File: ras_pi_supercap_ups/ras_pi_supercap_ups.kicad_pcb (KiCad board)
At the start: 2 copper layers, 16 parts, among them J1 Conn_01x03, J3 Conn_01x04, J4 Conn_01x04, J5 Conn_01x05, J6 Conn_01x05, J7 Barrel_Jack_Switch_Pin3Ring, Q1 SUD50P04-08, U1 ATtiny85-20P, U2 TL431LP, U3 TL431LP, U4 TL431LP, U5 TL431LP, U6 TL431LP, U7 LM2596S-5

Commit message: Updated part numbers
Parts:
- added C1: 10F, Capacitor_THT:CP_Radial_D12.5mm_P5.00mm, F.Cu at (32.9, 45.2)
- added C10: 22u 10V X7R, Capacitor_THT:C_Disc_D4.7mm_W2.5mm_P5.00mm, F.Cu at (210.2, 60.8)
- added C2: 10F, Capacitor_THT:CP_Radial_D12.5mm_P5.00mm, F.Cu at (48.6, 45.7)
- added C3: 10F, Capacitor_THT:CP_Radial_D12.5mm_P5.00mm, F.Cu at (64.0, 45.5)
- added C4: 10F, Capacitor_THT:CP_Radial_D12.5mm_P5.00mm, F.Cu at (79.1, 45.5)
- added C5: 10F, Capacitor_THT:CP_Radial_D12.5mm_P5.00mm, F.Cu at (95.8, 46.3)
- added C6: 10u 25V X7R, Capacitor_THT:C_Disc_D4.7mm_W2.5mm_P5.00mm, F.Cu at (202.5, 143.2)
- added C7: 22u 10V X7R, Capacitor_THT:C_Disc_D4.7mm_W2.5mm_P5.00mm, F.Cu at (181.5, 62.0)
- added C8: 22u 10V X7R, Capacitor_THT:C_Disc_D4.7mm_W2.5mm_P5.00mm, F.Cu at (124.5, 136.1)
- added C9: 22u 10V X7R, Capacitor_THT:C_Disc_D4.7mm_W2.5mm_P5.00mm, F.Cu at (139.5, 111.9)
- added D2: SA12A, Diode_THT:D_DO-15_P15.24mm_Horizontal, F.Cu at (118.2, 102.3)
- added D20: Green, LED_THT:LED_D5.0mm, F.Cu at (63.3, 98.6)
- added D3: SA12A, Diode_THT:D_DO-15_P15.24mm_Horizontal, F.Cu at (178.8, 70.6)
- added F1: Fuse_Small, Fuse:Fuse_BelFuse_0ZRE0005FF_L8.3mm_W3.8mm, F.Cu at (89.2, 147.1)
- added F2: Fuse_Small, Fuse:Fuse_BelFuse_0ZRE0005FF_L8.3mm_W3.8mm, F.Cu at (107.6, 144.9)
- added J2: OKR DC/DC, Connector_PinSocket_2.00mm:PinSocket_1x05_P2.00mm_Vertical, F.Cu at (130.0, 111.2)
- added J8: Conn_02x03_Odd_Even, Connector_PinHeader_2.54mm:PinHeader_2x03_P2.54mm_Vertical, F.Cu at (125.7, 111.0)
- added JP1: SolderJumper_2_Open, Jumper:SolderJumper-2_P1.3mm_Open_RoundedPad1.0x1.5mm, F.Cu at (109.7, 150.2)
- added JP2: SolderJumper_2_Open, Jumper:SolderJumper-2_P1.3mm_Open_RoundedPad1.0x1.5mm, F.Cu at (151.2, 105.5)
- added JP3: SolderJumper_2_Open, Jumper:SolderJumper-2_P1.3mm_Open_RoundedPad1.0x1.5mm, F.Cu at (105.4, 150.2)
- added JP4: SolderJumper_2_Open, Jumper:SolderJumper-2_P1.3mm_Open_RoundedPad1.0x1.5mm, F.Cu at (118.4, 110.7)
- added R1: 1k, Resistor_THT:R_Axial_DIN0207_L6.3mm_D2.5mm_P15.24mm_Horizontal, F.Cu at (137.0, 101.8)
- added R10: 267, Resistor_THT:R_Axial_DIN0516_L15.5mm_D5.0mm_P25.40mm_Horizontal, F.Cu at (106.8, 123.0)
- added R11: 10k, Resistor_THT:R_Axial_DIN0207_L6.3mm_D2.5mm_P15.24mm_Horizontal, F.Cu at (88.4, 139.2)
- added R12: 2.2k, Resistor_THT:R_Axial_DIN0207_L6.3mm_D2.5mm_P15.24mm_Horizontal, F.Cu at (88.8, 109.5)
- added R13: 1k, Resistor_THT:R_Axial_DIN0207_L6.3mm_D2.5mm_P15.24mm_Horizontal, F.Cu at (106.8, 114.8)
- added R14: 10k, Resistor_THT:R_Axial_DIN0207_L6.3mm_D2.5mm_P15.24mm_Horizontal, F.Cu at (117.8, 106.9)
- added R2: 1k, Resistor_THT:R_Axial_DIN0207_L6.3mm_D2.5mm_P15.24mm_Horizontal, F.Cu at (88.4, 123.0)
- added R20: 47k, Resistor_THT:R_Axial_DIN0207_L6.3mm_D2.5mm_P15.24mm_Horizontal, F.Cu at (44.0, 96.8)
- added R21: 47k, Resistor_THT:R_Axial_DIN0207_L6.3mm_D2.5mm_P15.24mm_Horizontal, F.Cu at (44.0, 100.9)
- added R3: 1k, Resistor_THT:R_Axial_DIN0207_L6.3mm_D2.5mm_P15.24mm_Horizontal, F.Cu at (88.8, 103.0)
- added R4: 1k, Resistor_THT:R_Axial_DIN0207_L6.3mm_D2.5mm_P15.24mm_Horizontal, F.Cu at (88.4, 118.9)
- added R5: 1k, Resistor_THT:R_Axial_DIN0207_L6.3mm_D2.5mm_P15.24mm_Horizontal, F.Cu at (88.4, 143.2)
- added R6: 1k, Resistor_THT:R_Axial_DIN0207_L6.3mm_D2.5mm_P15.24mm_Horizontal, F.Cu at (106.8, 127.0)
- added R7: 10 3W, Resistor_THT:R_Axial_DIN0516_L15.5mm_D5.0mm_P25.40mm_Horizontal, F.Cu at (106.8, 118.9)
- added R8: 10k, Resistor_THT:R_Axial_DIN0207_L6.3mm_D2.5mm_P15.24mm_Horizontal, F.Cu at (88.4, 114.8)
- added R9: 2.2k, Resistor_THT:R_Axial_DIN0207_L6.3mm_D2.5mm_P15.24mm_Horizontal, F.Cu at (88.4, 127.0)
- added TP1: TestPoint_Small, TestPoint:TestPoint_THTPad_D2.0mm_Drill1.0mm, F.Cu at (113.9, 150.4)
- added TP2: TestPoint_Small, TestPoint:TestPoint_THTPad_D2.0mm_Drill1.0mm, F.Cu at (118.0, 149.2)
- added TP3: TestPoint_Small, TestPoint:TestPoint_THTPad_D2.0mm_Drill1.0mm, F.Cu at (150.5, 129.8)
- added TP4: TestPoint_Small, TestPoint:TestPoint_THTPad_D2.0mm_Drill1.0mm, F.Cu at (122.0, 145.1)
- added TP5: TestPoint_Small, TestPoint:TestPoint_THTPad_D2.0mm_Drill1.0mm, F.Cu at (126.1, 145.1)
- added TP6: TestPoint_Small, TestPoint:TestPoint_THTPad_D2.0mm_Drill1.0mm, F.Cu at (170.2, 101.8)
- added TP7: TestPoint_Small, TestPoint:TestPoint_THTPad_D2.0mm_Drill1.0mm, F.Cu at (151.0, 109.3)
- added TP8: TestPoint_Small, TestPoint:TestPoint_THTPad_D2.0mm_Drill1.0mm, F.Cu at (118.0, 145.1)
- added TP9: TestPoint_Small, TestPoint:TestPoint_THTPad_D2.0mm_Drill1.0mm, F.Cu at (122.0, 149.2)
- added U8: ATtiny85-20P, Package_DIP:DIP-8_W7.62mm, F.Cu at (98.7, 148.5)
- J3, J4: value Conn_01x04 -> Conn_01x05; footprint Connector_PinHeader_2.54mm:PinHeader_1x04_P2.54mm_Vertical -> Connector_PinHeader_2.54mm:PinHeader_1x05_P2.54mm_Vertical
- J5: value Conn_01x05 -> Barrel_Jack_Switch_Pin3Ring; footprint Connector_PinHeader_2.54mm:PinHeader_1x05_P2.54mm_Vertical -> Connector_BarrelJack:BarrelJack_CUI_PJ-063AH_Horizontal
- J6: value Conn_01x05 -> Conn_01x04; footprint Connector_PinHeader_2.54mm:PinHeader_1x05_P2.54mm_Vertical -> Connector_PinHeader_2.54mm:PinHeader_1x04_P2.54mm_Vertical
- J7: value Barrel_Jack_Switch_Pin3Ring -> Conn_01x04; footprint Connector_BarrelJack:BarrelJack_CUI_PJ-063AH_Horizontal -> Connector_PinHeader_2.54mm:PinHeader_1x04_P2.54mm_Vertical
- Q1: value SUD50P04-08 -> IRF5305; footprint Package_TO_SOT_SMD:TO-252-2 -> Package_TO_SOT_THT:TO-220-3_Vertical
- U1: value ATtiny85-20P -> KA431AZTA; footprint Package_DIP:DIP-8_W7.62mm -> Package_TO_SOT_THT:TO-92_Inline
- U2, U3, U4, U5: value TL431LP -> KA431AZTA
- U6: value TL431LP -> LM2596S-5; footprint Package_TO_SOT_THT:TO-92_Inline -> Package_TO_SOT_SMD:TO-263-5_TabPin3
- U7: value LM2596S-5 -> L7805; footprint Package_TO_SOT_SMD:TO-263-5_TabPin3 -> Package_TO_SOT_THT:TO-220-3_Vertical
- moved D1 156.9 mm to (257.8, 114.7)
- moved D5 146.8 mm to (257.5, 79.5)
- moved J1 42.1 mm to (144.7, 33.0), turned to 90 degrees
- moved J6 37.9 mm to (121.5, 32.9), turned to 90 degrees
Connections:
- D5 pad 2: Net-(R1-Pad1) -> Net-(C1-Pad1)
- J3 pad 1: VIN -> POW_OUT
- J3 pad 3: GND -> I2C_SCL
- J3 pad 4: Net-(J3-Pad4) -> I2C_SDA
- J4 pad 1: VIN -> POW_OUT
- J4 pad 3: GND -> I2C_SCL
- J4 pad 4: Net-(J4-Pad4) -> I2C_SDA
- J5 pad 1: POW_OUT -> VIN
- J5 pad 2: GND -> unconnected-(J5-Pad2)
- J6 pad 1: POW_OUT -> VIN
- J6 pad 3: I2C_SCL -> GND
- J6 pad 4: I2C_SDA -> Net-(J6-Pad4)
- J7 pad 2: unconnected-(J7-Pad2) -> GND
- U1 pad 1: RESET -> Net-(C1-Pad1)
- U1 pad 2: VIN_SENSE -> Net-(C1-Pad1)
- U1 pad 3: UPS_SENSE -> Net-(C1-Pad2)
- U2 pad 1: Net-(R1-Pad1) -> Net-(C1-Pad2)
- U2 pad 2: Net-(R1-Pad1) -> Net-(C1-Pad2)
- U5 pad 3: Net-(R4-Pad2) -> GND
- U6 pad 1: Net-(R4-Pad2) -> Net-(C6-Pad1)
- U6 pad 2: Net-(R4-Pad2) -> +5V
- U7 pad 1: Net-(F2-Pad2) -> Net-(C6-Pad1)
- U7 pad 2: +5V -> GND
- U7 pad 3: GND -> Net-(JP1-Pad1)

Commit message: Started updating to SMT
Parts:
- removed F2: Fuse_Small, Fuse:Fuse_BelFuse_0ZRE0005FF_L8.3mm_W3.8mm
- added C11: 22u 10V X7R, Capacitor_SMD:C_0805_2012Metric, F.Cu at (109.7, 112.6)
- added C12: 0.1uF, Capacitor_SMD:C_0805_2012Metric, F.Cu at (109.7, 109.6)
- added H1: MountingHole, MountingHole:MountingHole_2.7mm_M2.5, F.Cu at (54.0, 103.5)
- added H2: MountingHole, MountingHole:MountingHole_2.7mm_M2.5, F.Cu at (114.2, 104.4)
- added H3: MountingHole, MountingHole:MountingHole_2.7mm_M2.5, F.Cu at (53.4, 152.2)
- added H4: MountingHole, MountingHole:MountingHole_2.7mm_M2.5, F.Cu at (111.5, 152.5)
- added J10: Raspberry_Pi_2_3, Connector_PinSocket_2.54mm:PinSocket_2x20_P2.54mm_Vertical, B.Cu at (59.6, 105.2)
- added J9: LEDs and Buttons, Connector_PinHeader_2.54mm:PinHeader_1x08_P2.54mm_Vertical, F.Cu at (16.7, 114.8)
- added U9: STC8H1K08, Package_SO:TSSOP-20_4.4x5mm_P0.5mm, F.Cu at (103.1, 111.3)
- C10, C6, C7, C8, C9: footprint Capacitor_THT:C_Disc_D4.7mm_W2.5mm_P5.00mm -> Capacitor_SMD:C_0805_2012Metric
- D1, D5: value 1N5820 -> B340LA-13-F; footprint Diode_THT:D_DO-201AD_P15.24mm_Horizontal -> Diode_SMD:D_SMA
- D2, D3: value SA12A -> PTVSHC3D15VUH; footprint Diode_THT:D_DO-15_P15.24mm_Horizontal -> Diode_SMD:D_SOD-323
- D20: footprint LED_THT:LED_D5.0mm -> LED_SMD:LED_0805_2012Metric
- F1: footprint Fuse:Fuse_BelFuse_0ZRE0005FF_L8.3mm_W3.8mm -> Fuse:Fuse_1206_3216Metric
- Q1: footprint Package_TO_SOT_THT:TO-220-3_Vertical -> Package_TO_SOT_SMD:TO-263-2
- R1, R2, R3, R4, R5: footprint Resistor_THT:R_Axial_DIN0207_L6.3mm_D2.5mm_P15.24mm_Horizontal -> Resistor_SMD:R_1206_3216Metric
- R10: footprint Resistor_THT:R_Axial_DIN0516_L15.5mm_D5.0mm_P25.40mm_Horizontal -> Resistor_SMD:R_0805_2012Metric
- R11, R12, R13, R14, R20, R21, R6, R8, R9: footprint Resistor_THT:R_Axial_DIN0207_L6.3mm_D2.5mm_P15.24mm_Horizontal -> Resistor_SMD:R_0805_2012Metric
- moved D5 180.9 mm to (81.1, 119.8)
- moved D1 152.9 mm to (105.0, 118.0)
- moved J6 151.9 mm to (15.2, 141.4)
- moved J7 142.6 mm to (18.8, 100.6)
- moved J1 139.9 mm to (17.7, 91.5)
- moved C10 132.0 mm to (99.5, 132.6)
- moved C1 124.0 mm to (111.0, 141.6), turned to 180 degrees
- moved C6 123.8 mm to (80.0, 124.6), turned to -90 degrees
- moved J4 119.3 mm to (25.0, 122.9)
- moved J3 115.0 mm to (17.9, 121.7)
- moved Q1 113.0 mm to (57.3, 119.0), turned to 90 degrees
- moved JP2 109.6 mm to (43.3, 86.2)
- moved C7 107.8 mm to (94.6, 126.0)
- moved C2 107.8 mm to (97.9, 141.6), turned to 180 degrees
- moved U3 106.6 mm to (85.7, 151.8), turned to 180 degrees
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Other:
- board outline added: 85 x 56 mm

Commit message: Updates
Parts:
- removed J5: Barrel_Jack_Switch_Pin3Ring, Connector_BarrelJack:BarrelJack_CUI_PJ-063AH_Horizontal
- removed JP2: SolderJumper_2_Open, Jumper:SolderJumper-2_P1.3mm_Open_RoundedPad1.0x1.5mm
- removed R10: 267, Resistor_SMD:R_0805_2012Metric
- added J12: 171826-4, raspberrypi_supercap_ups_lib:TE_171826-4, F.Cu at (111.2, 128.1)
- J1: value Conn_01x03 -> Raspberry_Pi_2_3; footprint Connector_PinHeader_2.54mm:PinHeader_1x03_P2.54mm_Vertical -> Connector_PinSocket_2.54mm:PinSocket_2x20_P2.54mm_Vertical; moved to B.Cu
- J10: value Raspberry_Pi_2_3 -> Conn_01x03; footprint Connector_PinSocket_2.54mm:PinSocket_2x20_P2.54mm_Vertical -> Connector_PinHeader_2.54mm:PinHeader_1x03_P2.54mm_Vertical
- J2: value OKR DC/DC -> Raspberry_Pi_2_3; footprint Connector_PinSocket_2.00mm:PinSocket_1x05_P2.00mm_Vertical -> Connector_PinSocket_2.54mm:PinSocket_2x20_P2.54mm_Vertical; moved to B.Cu
- JP1, JP3, JP4: moved to B.Cu
- moved R7 109.2 mm to (157.0, 100.8), turned to -90 degrees
- moved U7 76.5 mm to (70.5, 132.7)
- moved J8 72.7 mm to (110.5, 108.9)
- moved TP7 63.6 mm to (130.4, 143.3)
- moved TP3 57.3 mm to (130.4, 149.5)
- moved TP6 57.1 mm to (133.7, 143.6)
- moved JP1 45.6 mm to (73.6, 126.8), turned to 180 degrees
- moved D2 44.9 mm to (89.0, 117.9)
- moved J1 42.7 mm to (58.3, 104.8), turned to -90 degrees
- moved U8 39.9 mm to (30.0, 124.9)
- moved J10 39.2 mm to (95.9, 90.3)
- moved J3 37.2 mm to (53.0, 109.4)
- moved JP3 36.9 mm to (77.9, 126.8), turned to 180 degrees
- moved J2 34.2 mm to (58.3, 112.4), turned to -90 degrees
- moved D3 22.8 mm to (72.8, 122.2)
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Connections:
- J1 pad 1: Net-(D1-Pad1) -> +3V3
- J1 pad 2: Net-(J1-Pad2) -> POW_OUT
- J1 pad 3: GND -> I2C_SCL
- J10 pad 1: unconnected-(J10-Pad1) -> Net-(D1-Pad1)
- J10 pad 2: POW_OUT -> Net-(J10-Pad2)
- J10 pad 3: I2C_SCL -> GND
- J2 pad 1: unconnected-(J2-Pad1) -> +3V3
- J2 pad 2: Net-(C6-Pad1) -> POW_OUT
- J2 pad 3: GND -> I2C_SCL
- J2 pad 4: Net-(J2-Pad4) -> POW_OUT
- J2 pad 5: Net-(J2-Pad5) -> I2C_SDA
- R7 pad 1: Net-(J1-Pad2) -> Net-(J10-Pad2)
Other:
- board size 85 x 56 mm -> 65 x 56 mm

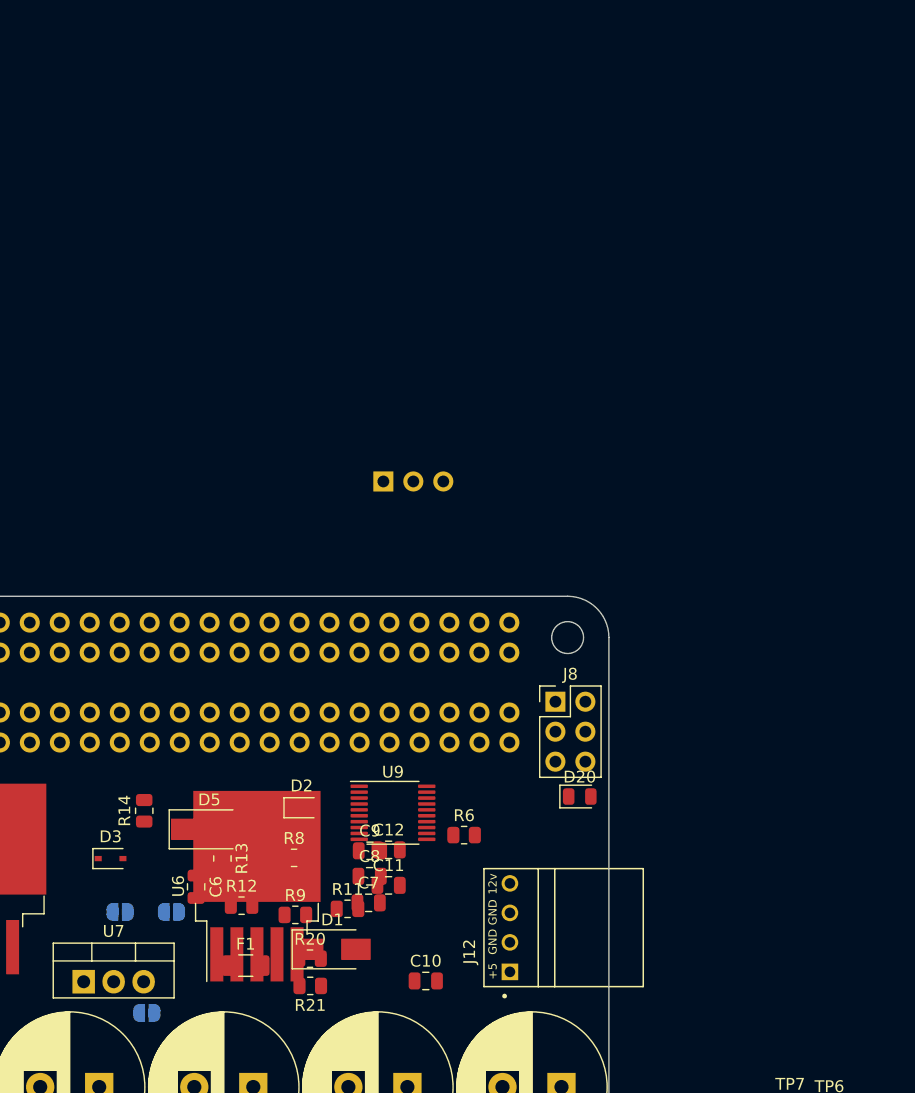
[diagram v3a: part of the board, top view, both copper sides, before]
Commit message: Added simple buck converter
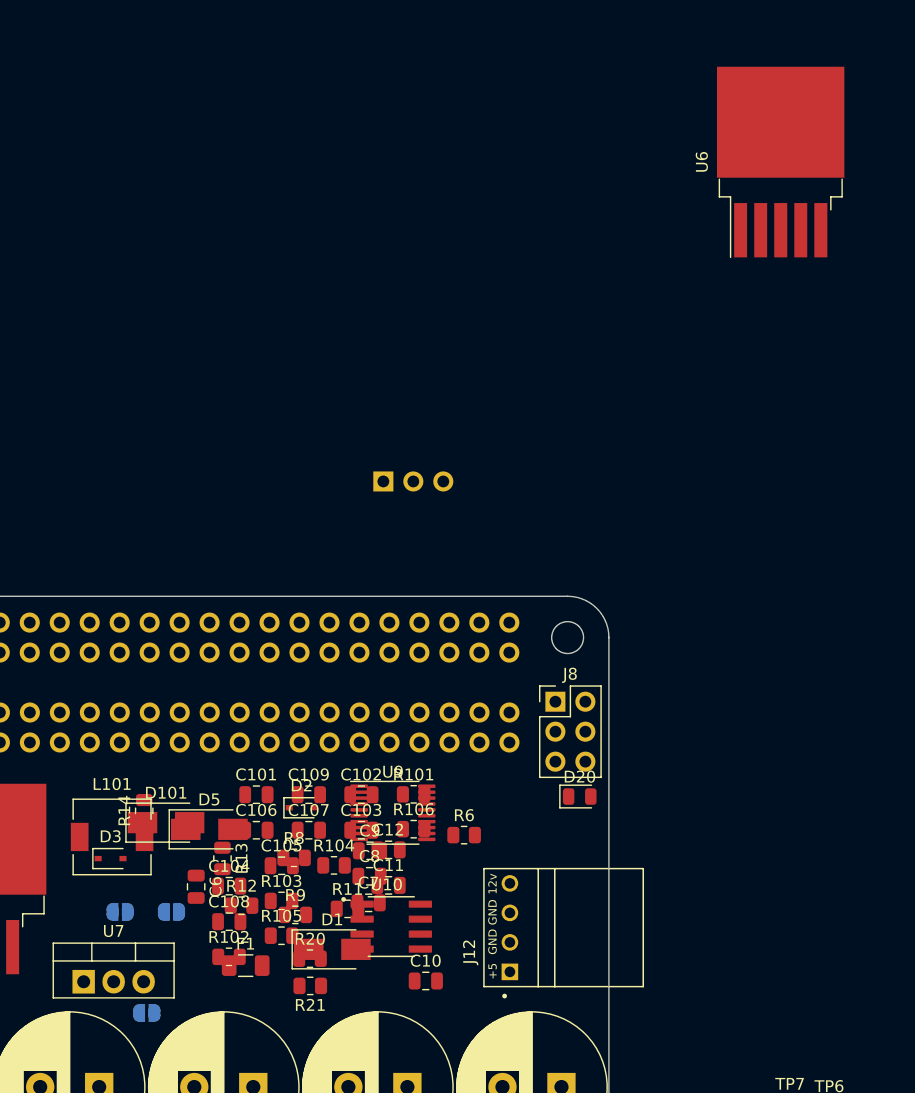
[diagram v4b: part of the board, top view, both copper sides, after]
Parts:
- added C101: 4.7u, Capacitor_SMD:C_0805_2012Metric, F.Cu at (85.1, 116.8)
- added C102: 4.7u, Capacitor_SMD:C_0805_2012Metric, F.Cu at (94.0, 116.8)
- added C103: 0.01u, Capacitor_SMD:C_0805_2012Metric, F.Cu at (94.0, 119.8)
- added C104: 0.1u, Capacitor_SMD:C_0805_2012Metric, F.Cu at (82.8, 124.6)
- added C105: 0.01u, Capacitor_SMD:C_0805_2012Metric, F.Cu at (87.3, 122.8)
- added C106: 1000p, Capacitor_SMD:C_0805_2012Metric, F.Cu at (85.1, 119.8)
- added C107: 47p, Capacitor_SMD:C_0805_2012Metric, F.Cu at (89.6, 119.8)
- added C108: 47u, Capacitor_SMD:C_0805_2012Metric, F.Cu at (82.8, 127.6)
- added C109: 47u, Capacitor_SMD:C_0805_2012Metric, F.Cu at (89.6, 116.8)
- added D101: B340A, Diode_SMD:D_SMA, F.Cu at (77.5, 119.2)
- added L101: 6.8uH, Inductor_SMD:L_6.3x6.3_H3, F.Cu at (72.9, 120.4)
- added R101: 332k, Resistor_SMD:R_0805_2012Metric, F.Cu at (98.5, 116.8)
- added R102: 68.1k, Resistor_SMD:R_0805_2012Metric, F.Cu at (82.8, 130.6)
- added R103: 29.4k, Resistor_SMD:R_0805_2012Metric, F.Cu at (87.3, 125.8)
- added R104: 0, Resistor_SMD:R_0805_2012Metric, F.Cu at (91.7, 122.8)
- added R105: 10.2k, Resistor_SMD:R_0805_2012Metric, F.Cu at (87.3, 128.8)
- added R106: 3.24k, Resistor_SMD:R_0805_2012Metric, F.Cu at (98.5, 119.7)
- added U10: TPS54331DR, raspberrypi_supercap_ups_lib:SOIC127P599X175-8N, F.Cu at (96.6, 128.0)
- moved U6 75.7 mm to (129.6, 63.2)

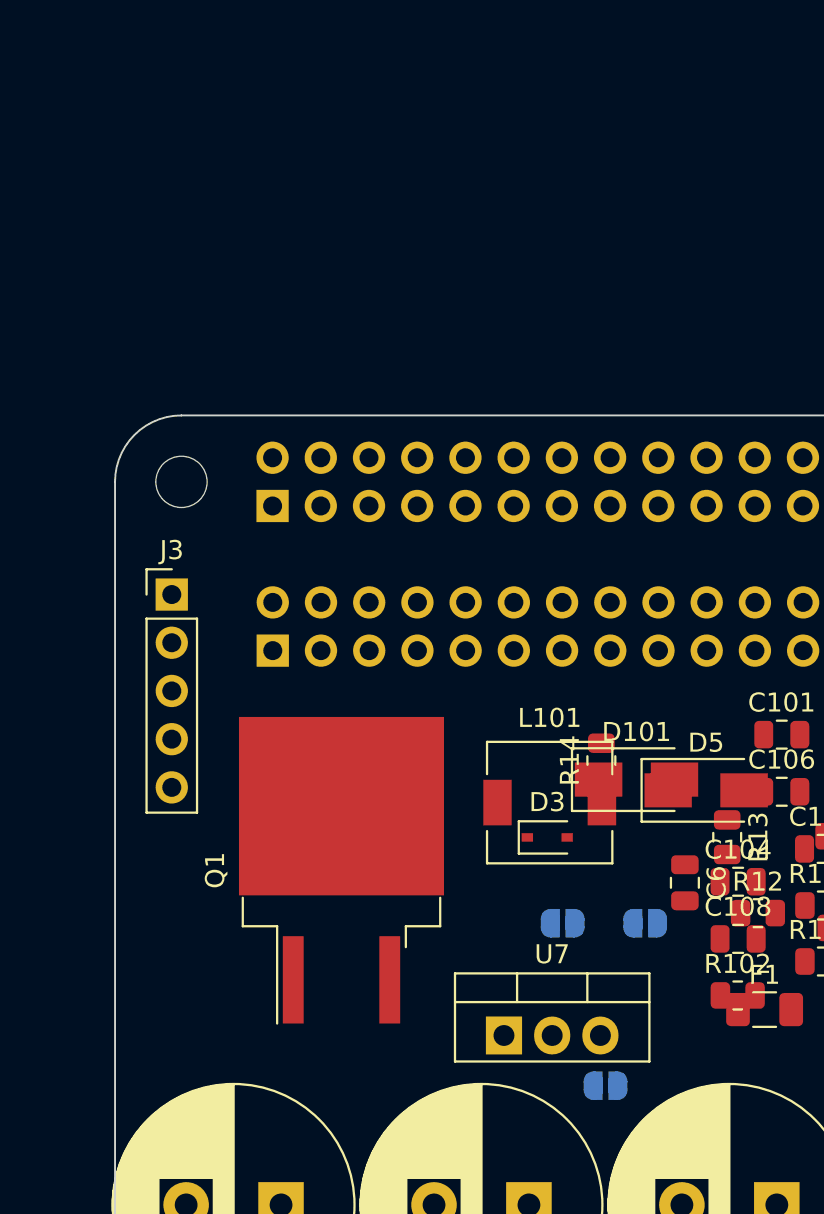
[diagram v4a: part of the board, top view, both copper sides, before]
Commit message: added 3d model
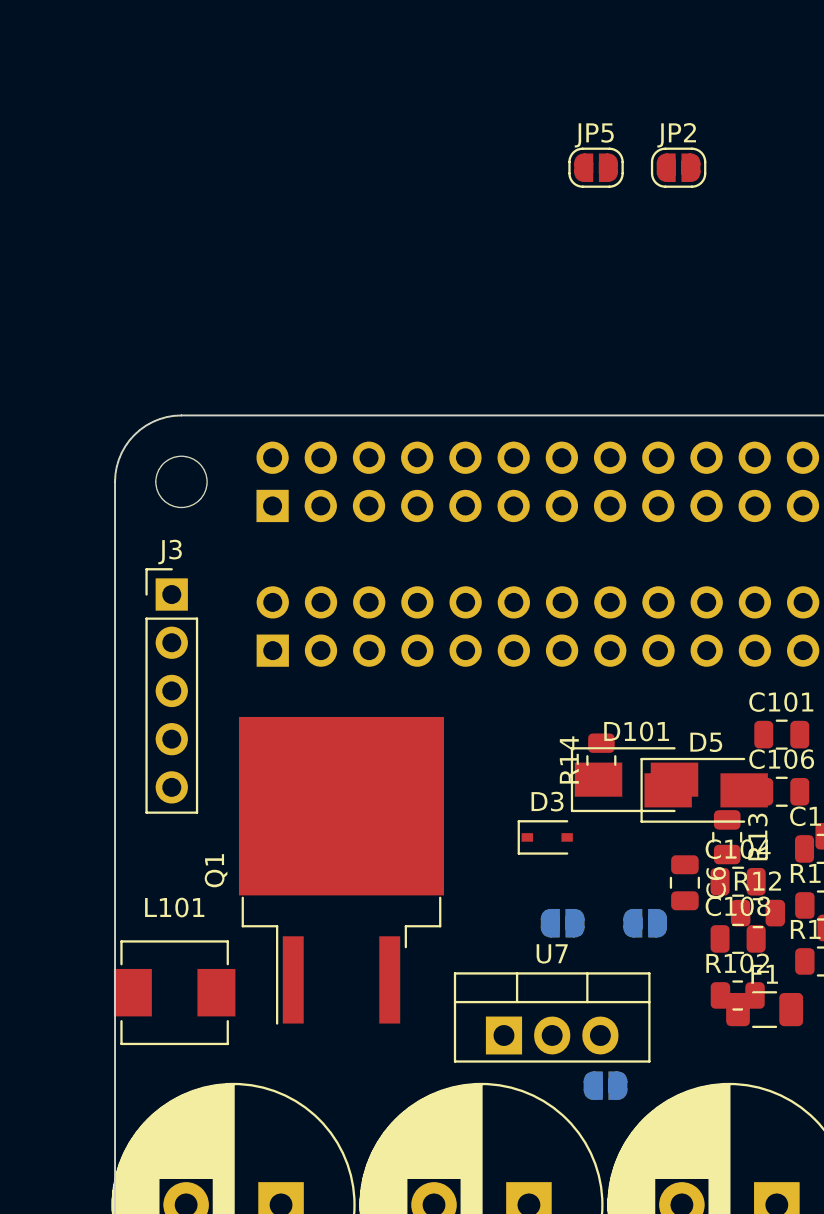
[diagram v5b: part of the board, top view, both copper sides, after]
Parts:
- added JP2: SolderJumper_2_Open, Jumper:SolderJumper-2_P1.3mm_Open_RoundedPad1.0x1.5mm, F.Cu at (79.7, 87.0)
- added JP5: SolderJumper_2_Open, Jumper:SolderJumper-2_P1.3mm_Open_RoundedPad1.0x1.5mm, F.Cu at (75.3, 87.0)
- C103: value 0.01u -> 4.7n
- C106: value 1000p -> 4.7n
- C107: value 47p -> 39p
- C108, C109: value 47u -> 33u
- C12: value 0.1uF -> 0.1u
- L101: footprint Inductor_SMD:L_6.3x6.3_H3 -> raspberrypi_supercap_ups_lib:Sunltech_SLO0530H
- R103: value 29.4k -> 49.9k
- moved L101 22.2 mm to (53.1, 130.4)
